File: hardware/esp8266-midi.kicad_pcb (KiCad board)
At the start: 2 copper layers, 82 x 75 mm, 31 parts, among them J1 MIDI in, J2 MIDI out, J3 TTL-232R-3V3 connector, J4 Bat+, J5 Bat-, J6 MIDI through, J7 Debug serial out, U1 ESP-12E, U2 6N138, U3 LD1117S50TR_SOT223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

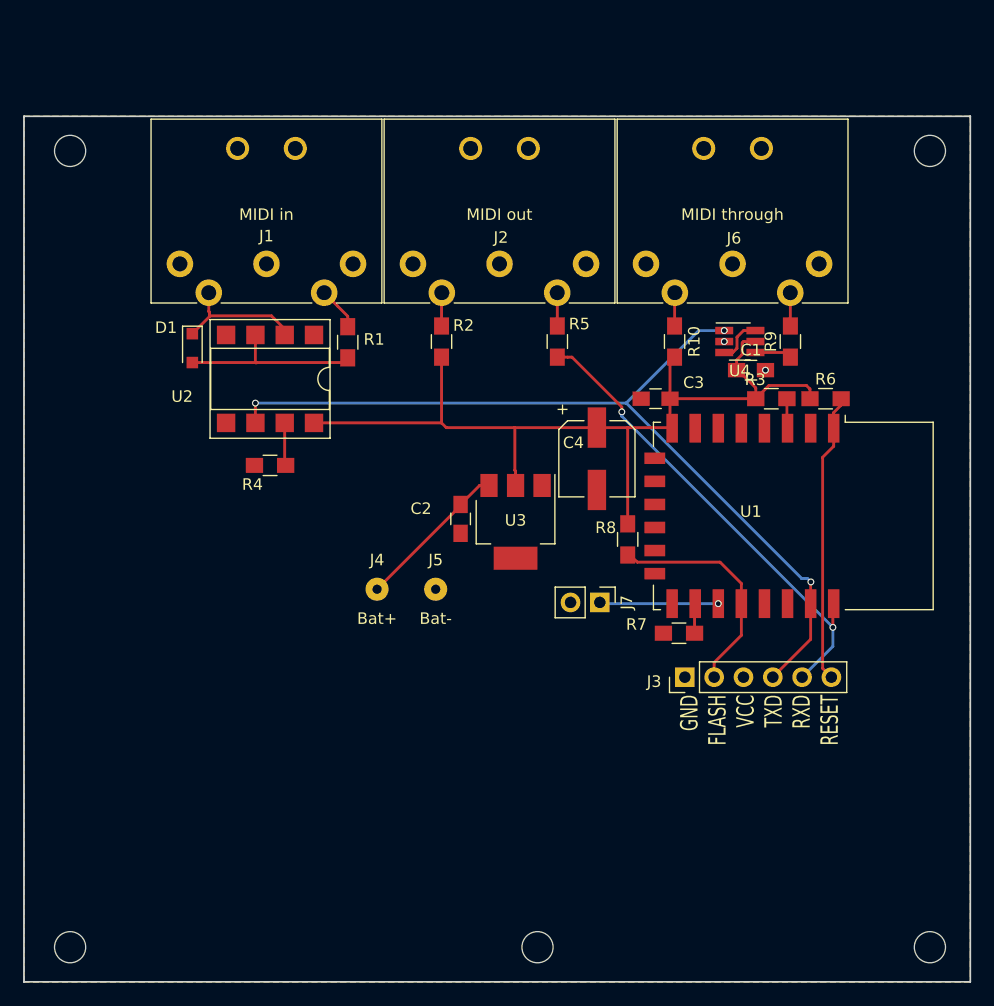
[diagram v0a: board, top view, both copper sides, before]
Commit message: New pcb: with midi through, all 3 connectors are now on the side
PCB will be mount flipped on top of enclosure. In future it will allow having
pcb mount push buttons + display available on front of enclosure.
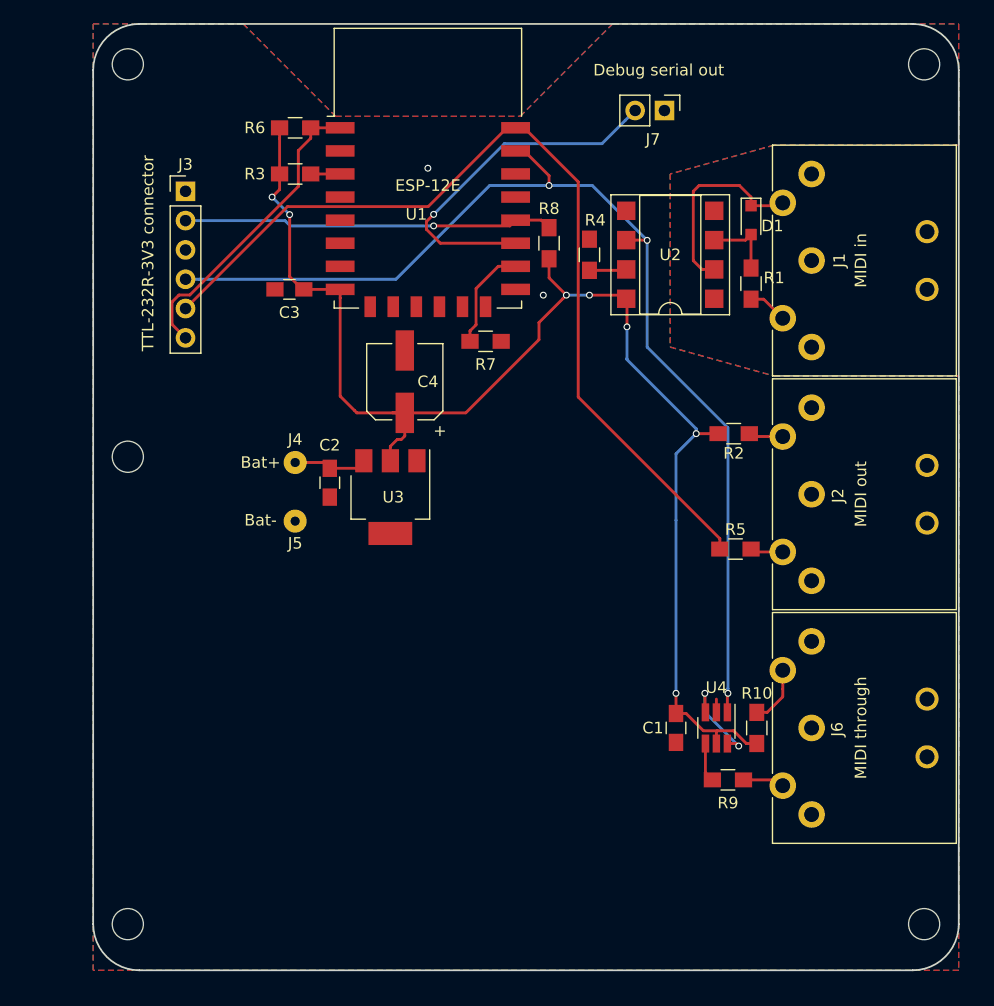
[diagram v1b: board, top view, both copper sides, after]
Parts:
- moved ? 76.5 mm to (187.5, 61.0), turned to 90 degrees
- moved ? 74.0 mm to (187.5, 135.5), turned to 90 degrees
- moved ? 69.9 mm to (118.5, 61.0), turned to 90 degrees
- moved ? 67.2 mm to (118.5, 135.5), turned to 90 degrees
- moved J3 60.4 mm to (123.5, 72.0), turned to 0 degrees
- moved ? 55.4 mm to (118.5, 95.0), turned to 90 degrees
- moved J1 55.3 mm to (177.8, 70.5), turned to 270 degrees
- moved R6 51.6 mm to (133.0, 66.5)
- moved D1 49.7 mm to (172.5, 74.5)
- moved R3 45.6 mm to (133.0, 70.5)
- moved U1 43.7 mm to (144.5, 70.0), turned to 0 degrees
- moved J7 43.0 mm to (165.0, 65.0)
- moved R9 38.4 mm to (170.5, 123.0), turned to 0 degrees
- moved J2 36.7 mm to (177.8, 90.8), turned to 270 degrees
- moved U2 36.3 mm to (165.5, 77.5), turned to 180 degrees
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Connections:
- J7 pad 1: Net-(J7-Pad1) -> GND
- J7 pad 2: GND -> Net-(J7-Pad2)
- U1 pad 17: Net-(J7-Pad1) -> Net-(J7-Pad2)
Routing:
- net VCC: track 78.6 -> 119.6 mm, vias 0 -> 7
- net UART0_TXD: track 41.6 -> 79.4 mm, vias 2 -> 0
- net Net-(J7-Pad2): track 0.00 -> 31.0 mm, vias 0 -> 1
- net UART0_RXD: track 77.1 -> 95.6 mm
- net Net-(J3-Pad2): track 20.0 -> 32.2 mm, vias 0 -> 1
- net Net-(J7-Pad1): track 10.3 -> 0.00 mm, vias 1 -> 0
- net Net-(D1-Pad2): track 16.2 -> 6.29 mm
- net Net-(C2-Pad1): track 13.6 -> 6.43 mm
- net Net-(R7-Pad1): track 3.24 -> 9.01 mm
- net Net-(D1-Pad1): track 11.6 -> 17.4 mm
- net Net-(U4-Pad3): track 4.06 -> 8.53 mm, vias 0 -> 2
- net Net-(J6-Pad4): track 2.89 -> 5.11 mm
- net Net-(J3-Pad6): track 25.1 -> 26.8 mm
- net GND: track 0.00 -> 1.15 mm
- net Net-(J6-Pad5): track 2.88 -> 3.61 mm
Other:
- board size 82 x 75 mm -> 75 x 82 mm
- board text removed: "GND FLASH VCC TXD RXD RESET"

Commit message: Misc: add some extra labels to have little more meaningful net names
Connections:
- net Net-(J3-Pad2) renamed FLASH_EN
- net Net-(J3-Pad6) renamed RESET
- net Net-(J7-Pad2) renamed UART1_TXD
